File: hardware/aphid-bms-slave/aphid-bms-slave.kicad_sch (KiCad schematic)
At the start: 3 parts, among them J1 Conn_01x15, J2 Conn_01x04, J3 Conn_01x04

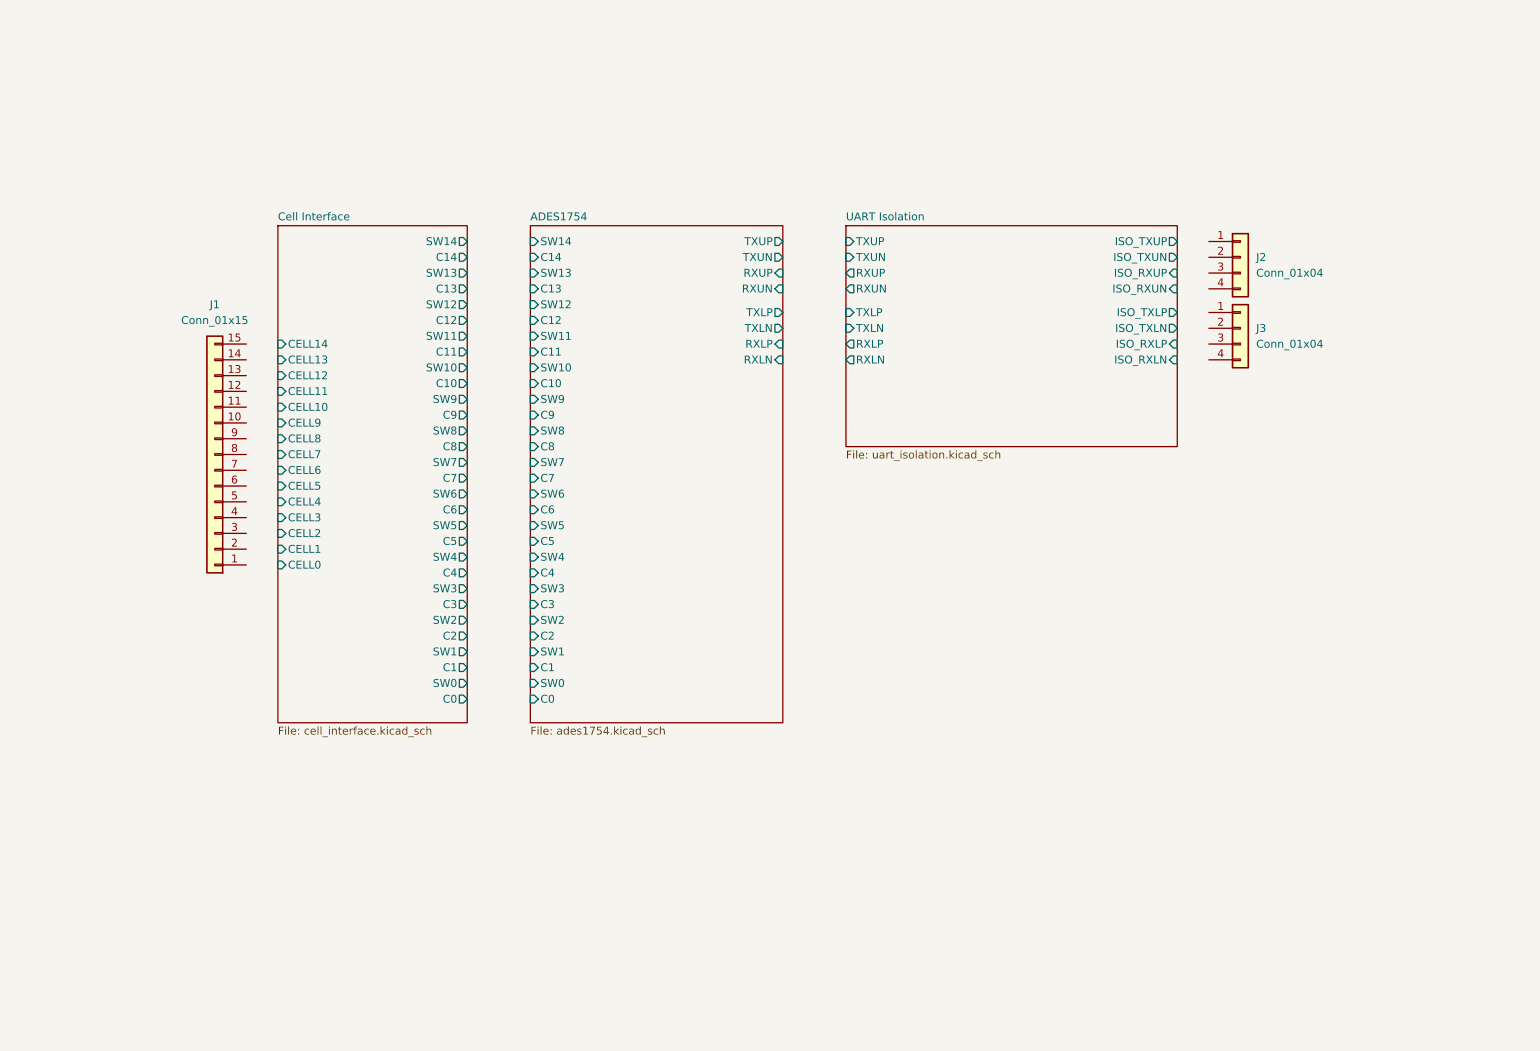
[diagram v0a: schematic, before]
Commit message: Worked on BMS slave schematic
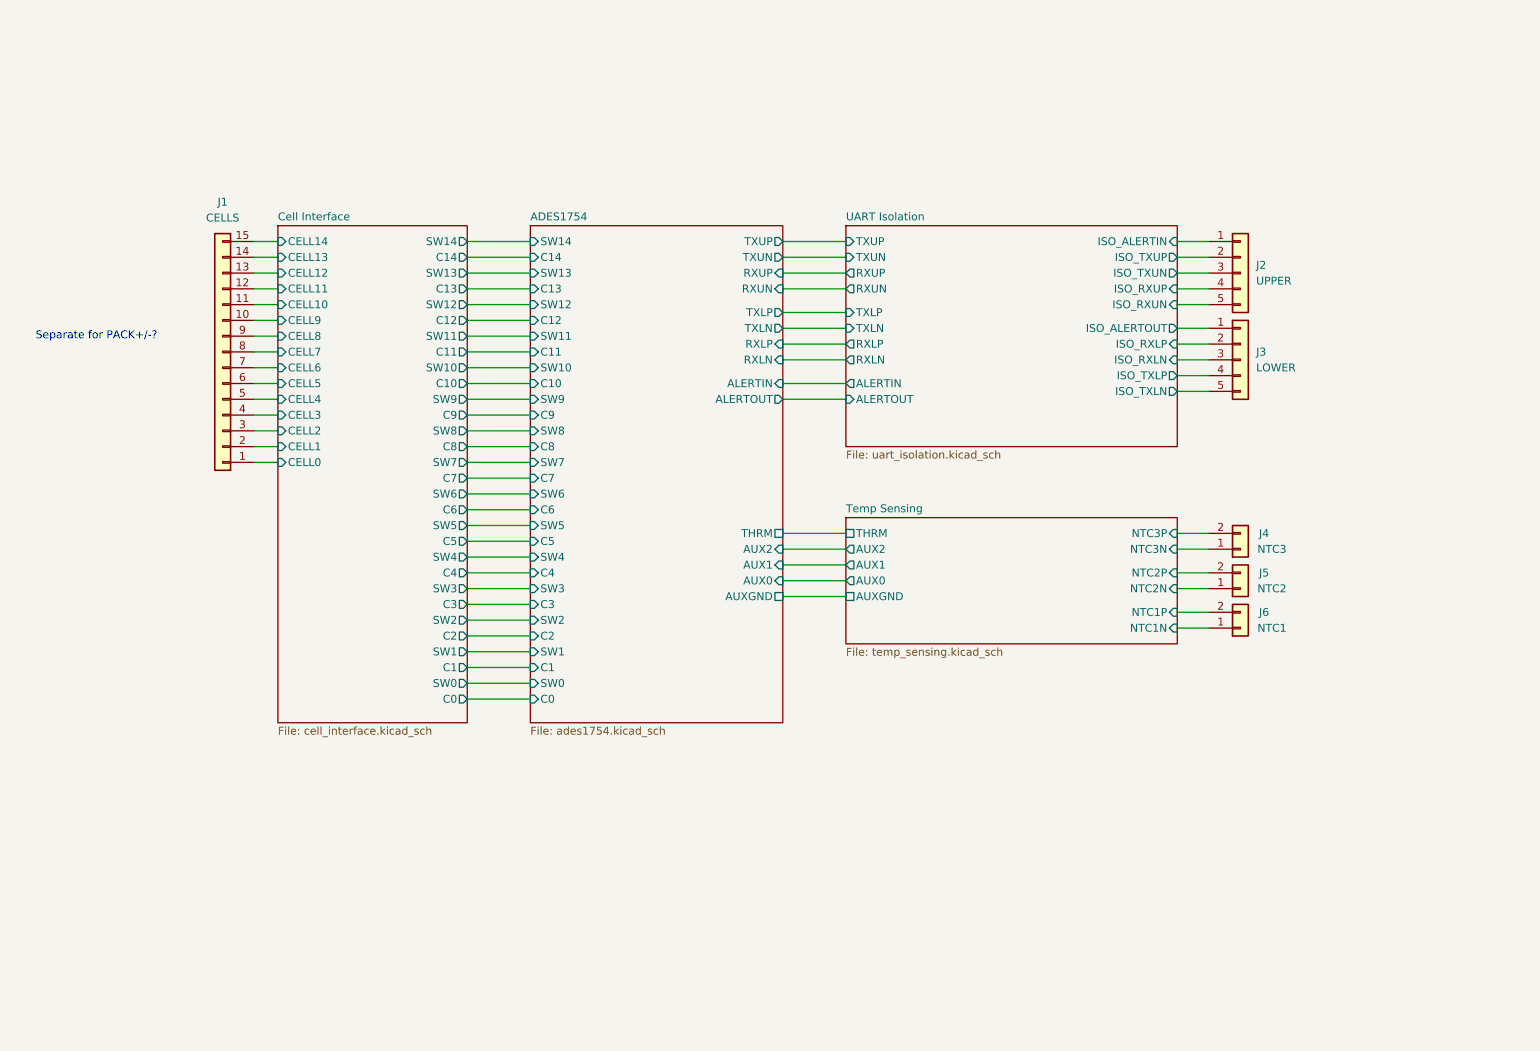
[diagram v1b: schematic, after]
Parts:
- added J4: NTC3, symbol Connector_Generic:Conn_01x02
- added J5: NTC2, symbol Connector_Generic:Conn_01x02
- added J6: NTC1, symbol Connector_Generic:Conn_01x02
- J1: value Conn_01x15 -> CELLS
- J2: value Conn_01x04 -> UPPER; symbol Connector_Generic:Conn_01x04 -> Connector_Generic:Conn_01x05
- J3: value Conn_01x04 -> LOWER; symbol Connector_Generic:Conn_01x04 -> Connector_Generic:Conn_01x05
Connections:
- net Cell Interface/CELL0: now also J1.1 (Pin_1)
- net Cell Interface/CELL1: now also J1.2 (Pin_2)
- net Cell Interface/CELL10: now also J1.11 (Pin_11)
- net Cell Interface/CELL11: now also J1.12 (Pin_12)
- net Cell Interface/CELL12: now also J1.13 (Pin_13)
- net Cell Interface/CELL13: now also J1.14 (Pin_14)
- net Cell Interface/CELL14: now also J1.15 (Pin_15)
- net Cell Interface/CELL2: now also J1.3 (Pin_3)
- net Cell Interface/CELL3: now also J1.4 (Pin_4)
- net Cell Interface/CELL4: now also J1.5 (Pin_5)
- net Cell Interface/CELL5: now also J1.6 (Pin_6)
- net Cell Interface/CELL6: now also J1.7 (Pin_7)
- net Cell Interface/CELL7: now also J1.8 (Pin_8)
- net Cell Interface/CELL8: now also J1.9 (Pin_9)
- net Cell Interface/CELL9: now also J1.10 (Pin_10)
- net UART Isolation/ISO_RXLN: now also J3.3 (Pin_3)
- net UART Isolation/ISO_RXLP: now also J3.2 (Pin_2)
- net UART Isolation/ISO_RXUN: now also J2.5 (Pin_5)
- net UART Isolation/ISO_RXUP: now also J2.4 (Pin_4)
- net UART Isolation/ISO_TXLN: now also J3.5 (Pin_5)
- net UART Isolation/ISO_TXLP: now also J3.4 (Pin_4)
- net UART Isolation/ISO_TXUN: now also J2.3 (Pin_3)
- net UART Isolation/ISO_TXUP: now also J2.2 (Pin_2)
- net UART Isolation/ISO_ALERTIN: now reaches J2.1 (Pin_1)
- net UART Isolation/ISO_ALERTOUT: now reaches J3.1 (Pin_1)
- new net Temp Sensing/NTC1N: J6.1 (Pin_1)
- new net Temp Sensing/NTC1P: J6.2 (Pin_2)
- new net Temp Sensing/NTC2N: J5.1 (Pin_1)
- new net Temp Sensing/NTC2P: J5.2 (Pin_2)
- new net Temp Sensing/NTC3N: J4.1 (Pin_1)
- new net Temp Sensing/NTC3P: J4.2 (Pin_2)
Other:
- added sheet Temp Sensing (temp_sensing.kicad_sch)
- sheet ADES1754 ports: added ALERTIN, ALERTOUT, AUX0, AUX1, AUX2, AUXGND, THRM; removed none
- sheet UART Isolation ports: added ALERTIN, ALERTOUT, ISO_ALERTIN, ISO_ALERTOUT; removed none
- note added: "Separate for PACK+/-?"
- moved on the sheet: J1

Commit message: Worked on BMS slave schematic and layout
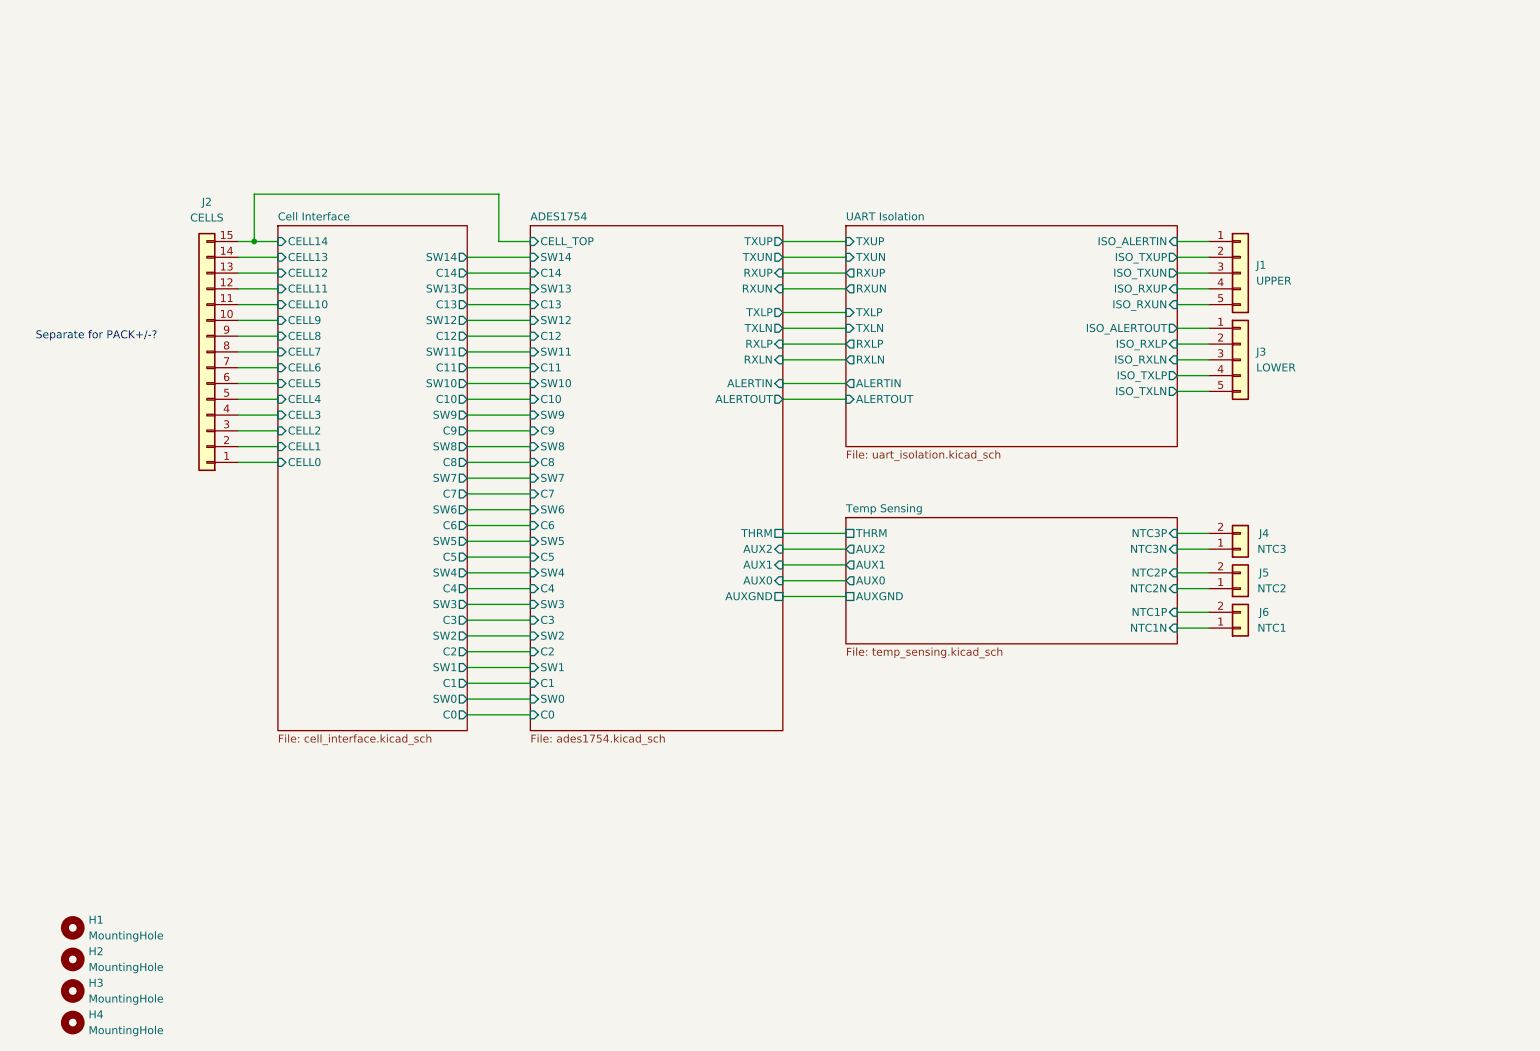
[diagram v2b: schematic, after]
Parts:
- added H1, H2, H3, H4: MountingHole, MountingHole:MountingHole_4.3mm_M4, symbol Mechanical:MountingHole
- J1: renamed from J2; footprint (none) -> Connector_PinHeader_2.54mm:PinHeader_1x05_P2.54mm_Vertical
- J2: renamed from J1; footprint (none) -> Connector_PinHeader_2.54mm:PinHeader_1x15_P2.54mm_Vertical
- J3: footprint (none) -> Connector_PinHeader_2.54mm:PinHeader_1x05_P2.54mm_Vertical
- J4, J5, J6: footprint (none) -> Connector_PinHeader_2.54mm:PinHeader_1x02_P2.54mm_Vertical
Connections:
- net Cell Interface/CELL14 renamed ADES1754/CELL_TOP
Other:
- sheet ADES1754 ports: added CELL_TOP; removed none
- moved on the sheet: J2

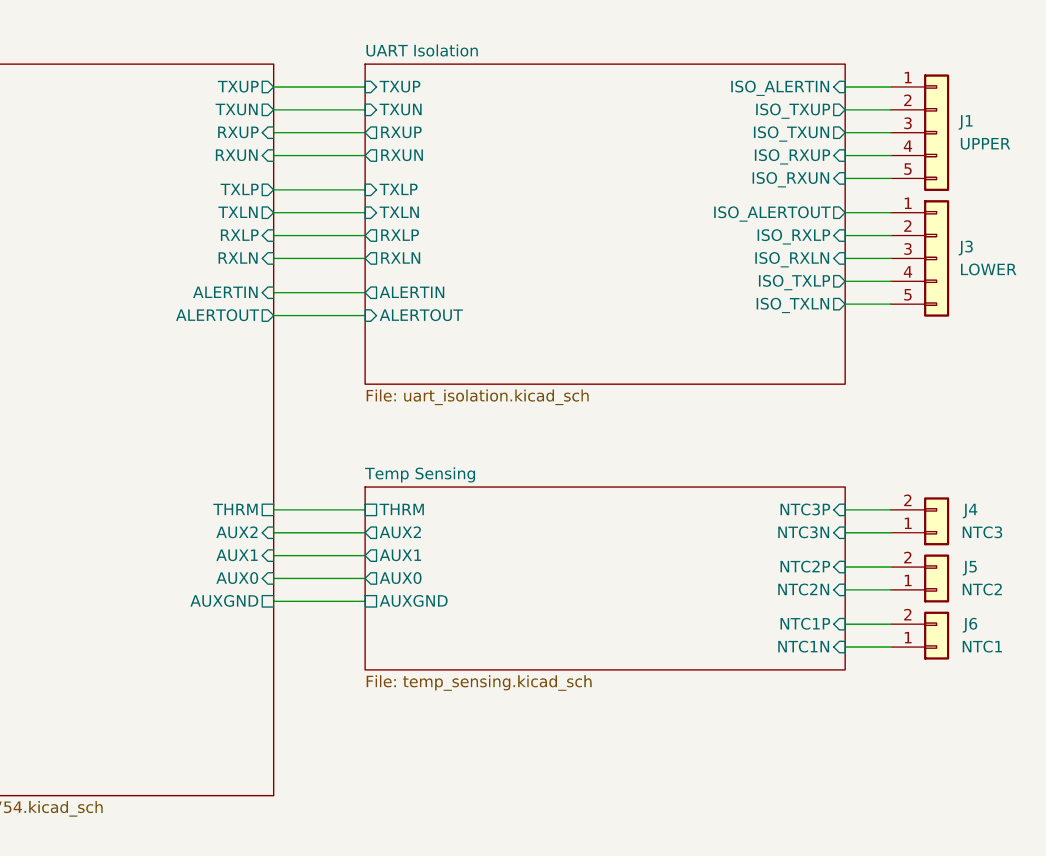
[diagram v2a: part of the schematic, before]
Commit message: Worked on BMS slave schematic and layout
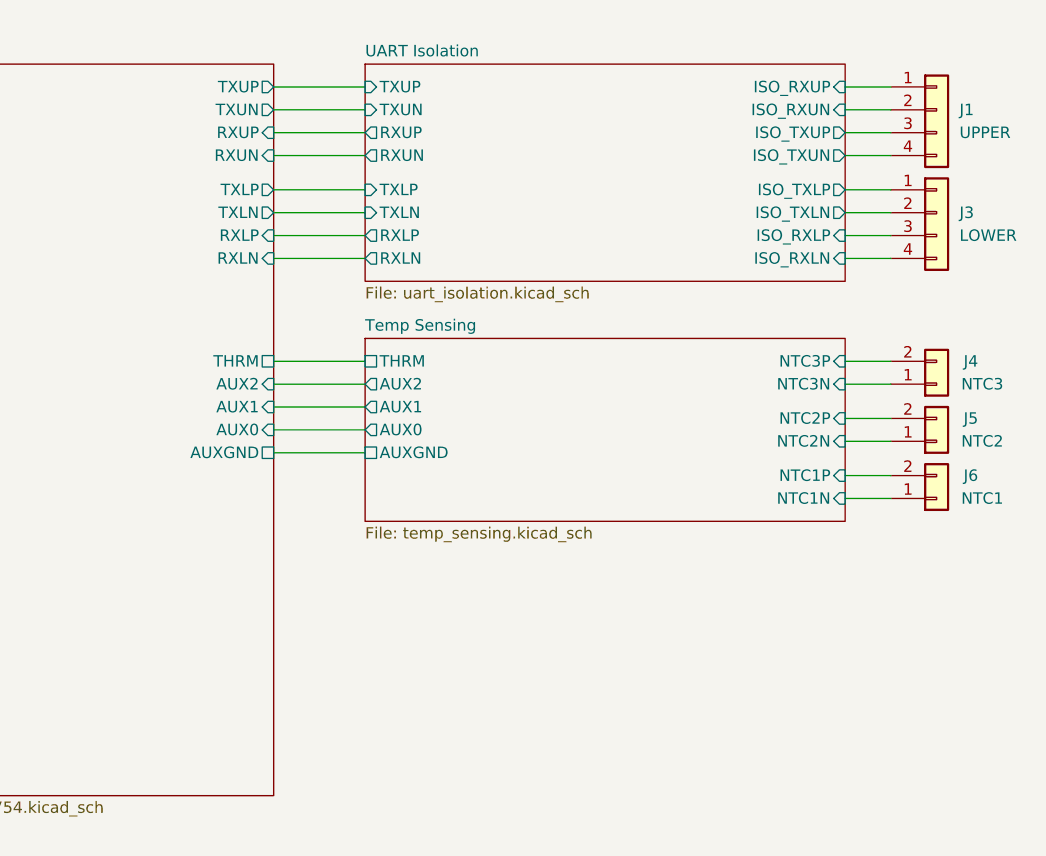
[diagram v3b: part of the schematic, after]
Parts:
- J1, J3: footprint Connector_PinHeader_2.54mm:PinHeader_1x05_P2.54mm_Vertical -> Connector_PinHeader_2.54mm:PinHeader_1x04_P2.54mm_Vertical; symbol Connector_Generic:Conn_01x05 -> Connector_Generic:Conn_01x04
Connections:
- net UART Isolation/ISO_ALERTIN is gone; now on net UART Isolation/ISO_RXUP: J1.1 (Pin_1)
- net UART Isolation/ISO_ALERTOUT is gone; now on net UART Isolation/ISO_TXLP: J3.1 (Pin_1)
- net UART Isolation/ISO_RXLN: now also J3.4 (Pin_4); no longer J3.3 (Pin_3)
- net UART Isolation/ISO_RXLP: now also J3.3 (Pin_3); no longer J3.2 (Pin_2)
- net UART Isolation/ISO_RXUN: now also J1.2 (Pin_2); no longer J1.5 (Pin_5)
- net UART Isolation/ISO_RXUP: no longer J1.4 (Pin_4)
- net UART Isolation/ISO_TXLN: now also J3.2 (Pin_2); no longer J3.5 (Pin_5)
- net UART Isolation/ISO_TXLP: no longer J3.4 (Pin_4)
- net UART Isolation/ISO_TXUN: now also J1.4 (Pin_4); no longer J1.3 (Pin_3)
- net UART Isolation/ISO_TXUP: now also J1.3 (Pin_3); no longer J1.2 (Pin_2)
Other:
- sheet ADES1754 ports: added none; removed ALERTIN, ALERTOUT
- sheet UART Isolation ports: added none; removed ALERTIN, ALERTOUT, ISO_ALERTIN, ISO_ALERTOUT
- moved on the sheet: J4, J5, J6

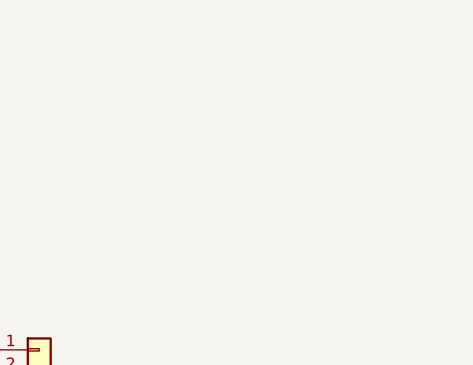
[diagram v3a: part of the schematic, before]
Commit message: BMS slave 1.0 done
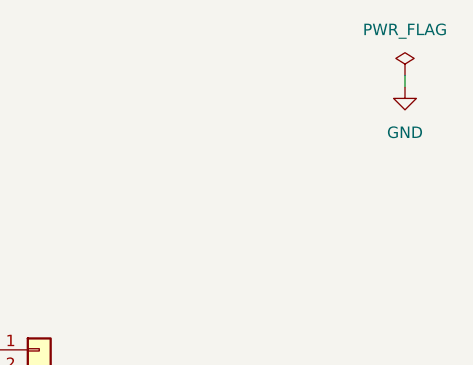
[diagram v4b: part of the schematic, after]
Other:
- company: (none) -> https://aphid-ev.se
- title: (none) -> aphid-ev BMS slave
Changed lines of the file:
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@@
 	(generator_version "8.0")
 	(paper "A4")
+	(title_block
+		(title "aphid-ev BMS slave")
+		(date "2024-07-23")
+		(rev "1.0")
+		(company "https://aphid-ev.se")
+	)
 	(junction
 		(at 73.66 54.61)
@@
 		(pts
 			(xy 107.95 74.93) (xy 118.11 74.93)
+		)
+		(stroke
+			(width 0)
+			(type default)
+		)
+	)
+	(wire
+		(pts
+			(xy 273.05 24.13) (xy 273.05 25.4)
 		)
 		(stroke
@@
 					(unit 1)
 				)
+			)
+		)
+	)
+	(symbol
+		(lib_id "power:GND")
+		(at 273.05 25.4 0)
+		(unit 1)
+		(exclude_from_sim no)
+		(in_bom yes)
+		(on_board yes)
+		(dnp no)
+		(fields_autoplaced yes)
+		(property "Reference" "#PWR044"
+			(at 273.05 31.75 0)
+			(effects
+				(font
+					(size 1.27 1.27)
+				)
+				(hide yes)
+			)
+		)
+		(property "Value" "GND"
+			(at 273.05 30.48 0)
+			(effects
+				(font
+					(size 1.27 1.27)
+				)
+			)
+		)
+		(property "Footprint" ""
+			(at 273.05 25.4 0)
+			(effects
+				(font
+					(size 1.27 1.27)
+				)
+				(hide yes)
+			)
+		)
+		(property "Datasheet" ""
+			(at 273.05 25.4 0)
+			(effects
+				(font
+					(size 1.27 1.27)
+				)
+				(hide yes)
+			)
+		)
+		(property "Description" "Power symbol creates a global label with name \"GND\" , ground"
+			(at 273.05 25.4 0)
+			(effects
+				(font
+					(size 1.27 1.27)
+				)
+				(hide yes)
+			)
+		)
+		(pin "1"
+		)
+		(instances
+			(project ""
+				(path "/36f5197f-5a2b-49d7-95ca-bb7937adb059"
+					(reference "#PWR044")
+					(unit 1)
+				)
+			)
+		)
+	)
+	(symbol
+		(lib_id "power:PWR_FLAG")
+		(at 273.05 24.13 0)
+		(unit 1)
+		(exclude_from_sim no)
+		(in_bom yes)
+		(on_board yes)
+		(dnp no)
+		(fields_autoplaced yes)
+		(property "Reference" "#FLG01"
+			(at 273.05 22.225 0)
+			(effects
+				(font
+					(size 1.27 1.27)
+				)
+				(hide yes)
+			)
+		)
+		(property "Value" "PWR_FLAG"
+			(at 273.05 19.05 0)
+			(effects
+				(font
+					(size 1.27 1.27)
+				)
+			)
+		)
+		(property "Footprint" ""
+			(at 273.05 24.13 0)
+			(effects
+				(font
+					(size 1.27 1.27)
+				)
+				(hide yes)
+			)
+		)
+		(property "Datasheet" "~"
+			(at 273.05 24.13 0)
+			(effects
+				(font
+					(size 1.27 1.27)
+				)
+				(hide yes)
+			)
+		)
+		(property "Description" "Special symbol for telling ERC where power comes from"
+			(at 273.05 24.13 0)
+			(effects
+				(font
+					(size 1.27 1.27)
+				)
+				(hide yes)
+			)
+		)
+		(pin "1"
+		)
+		(instances
+			(project ""
+				(path "/36f5197f-5a2b-49d7-95ca-bb7937adb059"
+					(reference "#FLG01")
+					(unit 1)
+				)
